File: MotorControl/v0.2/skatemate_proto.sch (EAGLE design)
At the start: 97 parts, among them IC1 REG1117, U1 DRV8301DCAR, U2 STM32F303XD/XELQFP64, X1 ABM3B

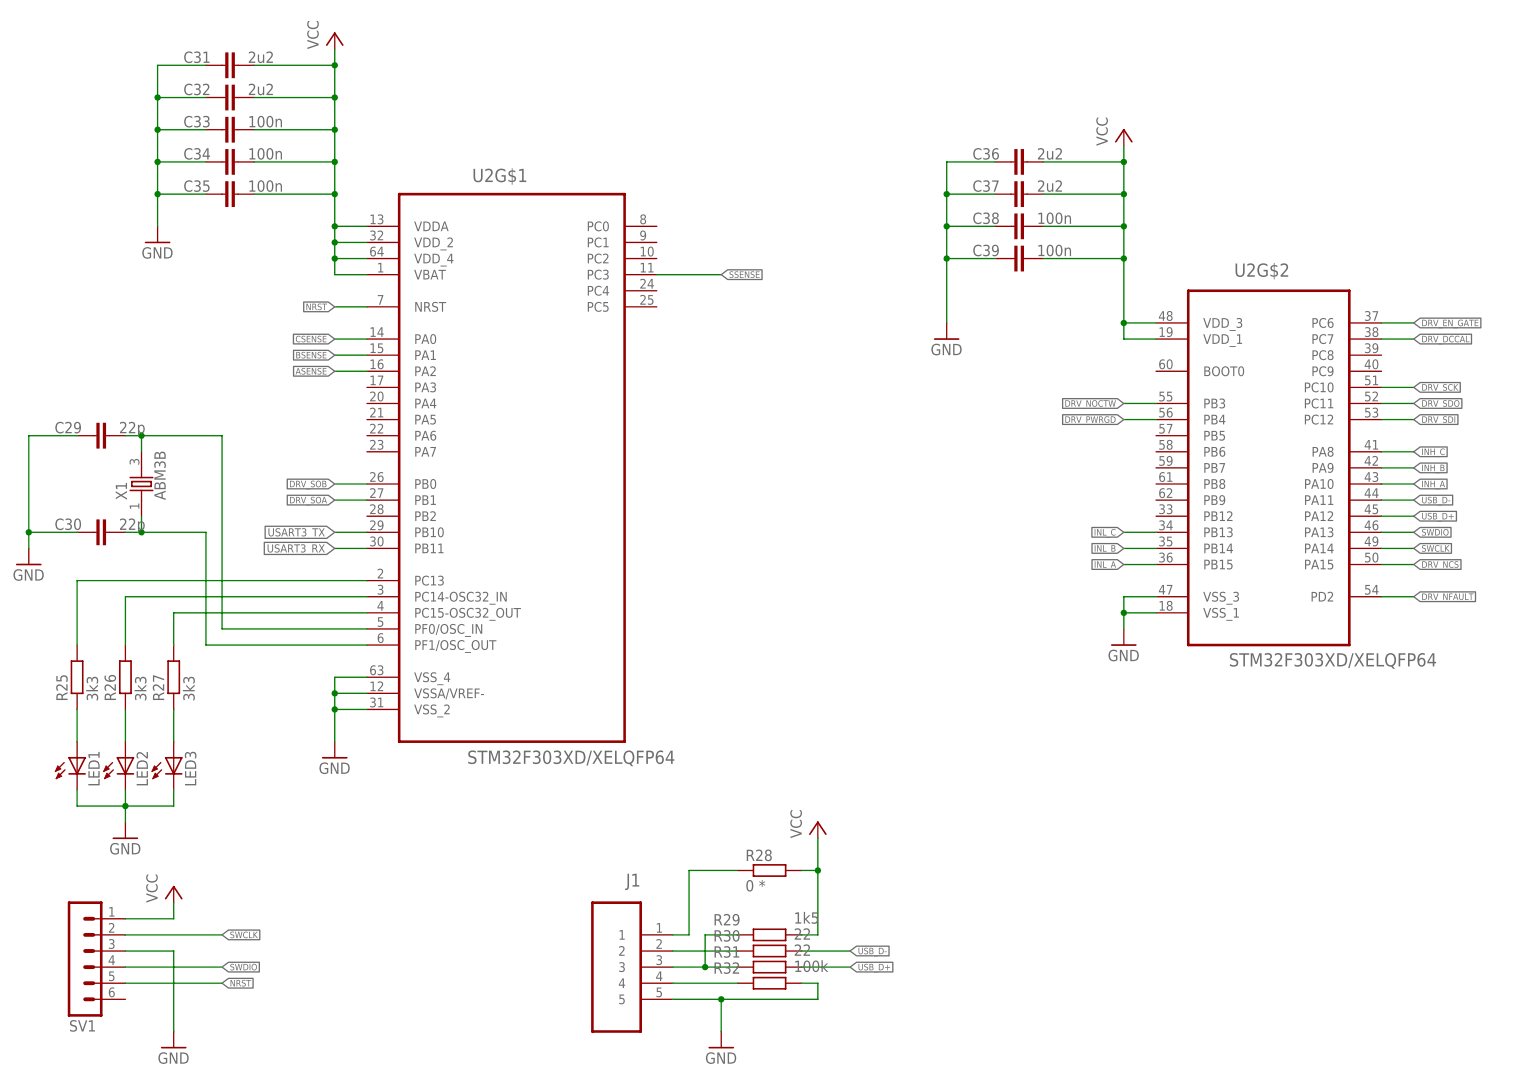
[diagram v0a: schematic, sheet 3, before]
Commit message: Add RFM module
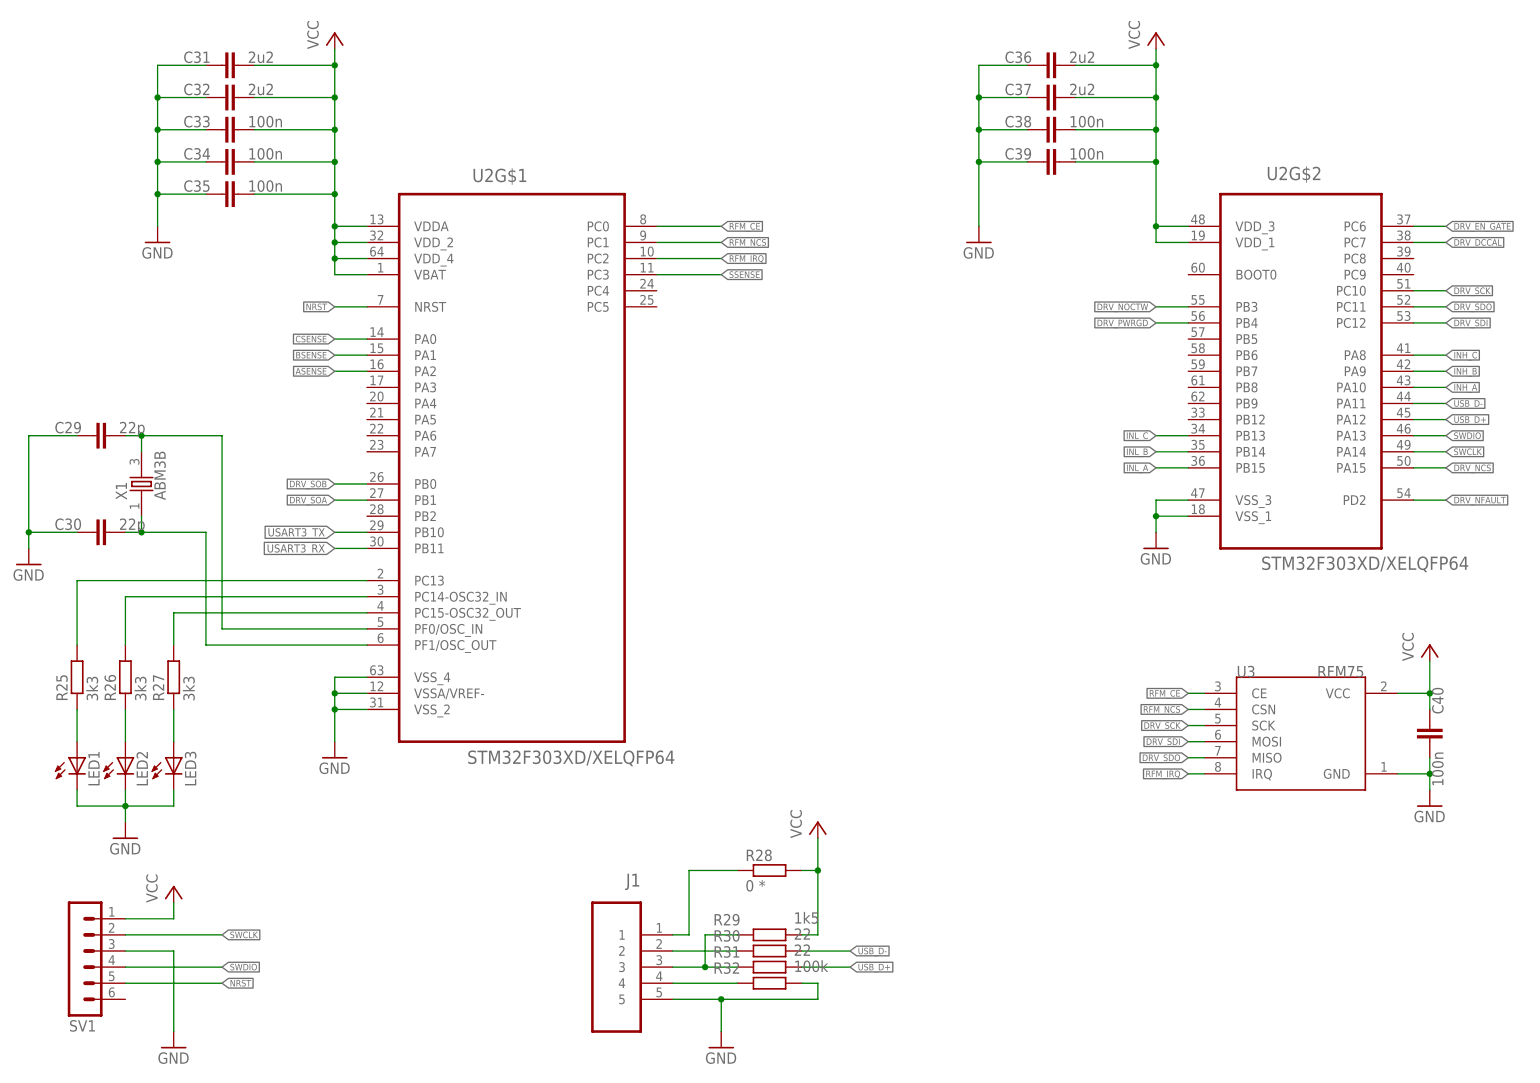
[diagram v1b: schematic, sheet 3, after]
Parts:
- added C40: 100n, skatemate:C-EUC0805
- added U3: RFM75, skatemate:RFM75
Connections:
- new net RFM_CE: U2G$1.PC0, U3.CE
- new net RFM_IRQ: U2G$1.PC2, U3.IRQ
- new net RFM_NCS: U2G$1.PC1, U3.CSN
- net DRV_SCK: now also U3.SCK
- net DRV_SDI: now also U3.MOSI
- net DRV_SDO: now also U3.MISO
- net GND: now also C40.2, U3.GND
- net VCC: now also C40.1, U3.VCC
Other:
- moved on the sheet: C36, C37, C38, C39, U2G$2

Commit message: finished all wires and first review
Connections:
- net RFM_CE: now also U2G$1.PC2; no longer U2G$1.PC0
- net RFM_IRQ: now also U2G$1.PC0; no longer U2G$1.PC2
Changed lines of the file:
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@@
 </segment>
 <segment>
-<pinref part="U2" gate="G$1" pin="PC0"/>
-<wire x1="101.6" y1="142.24" x2="111.76" y2="142.24" width="0.1524" layer="91"/>
-<label x="111.76" y="142.24" size="1.016" layer="95" xref="yes"/>
+<pinref part="U2" gate="G$1" pin="PC2"/>
+<wire x1="101.6" y1="137.16" x2="111.76" y2="137.16" width="0.1524" layer="91"/>
+<label x="111.76" y="137.16" size="1.016" layer="95" xref="yes"/>
 </segment>
 </net>
@@
 </segment>
 <segment>
-<pinref part="U2" gate="G$1" pin="PC2"/>
-<wire x1="101.6" y1="137.16" x2="111.76" y2="137.16" width="0.1524" layer="91"/>
-<label x="111.76" y="137.16" size="1.016" layer="95" xref="yes"/>
+<pinref part="U2" gate="G$1" pin="PC0"/>
+<wire x1="101.6" y1="142.24" x2="111.76" y2="142.24" width="0.1524" layer="91"/>
+<label x="111.76" y="142.24" size="1.016" layer="95" xref="yes"/>
 </segment>
 </net>

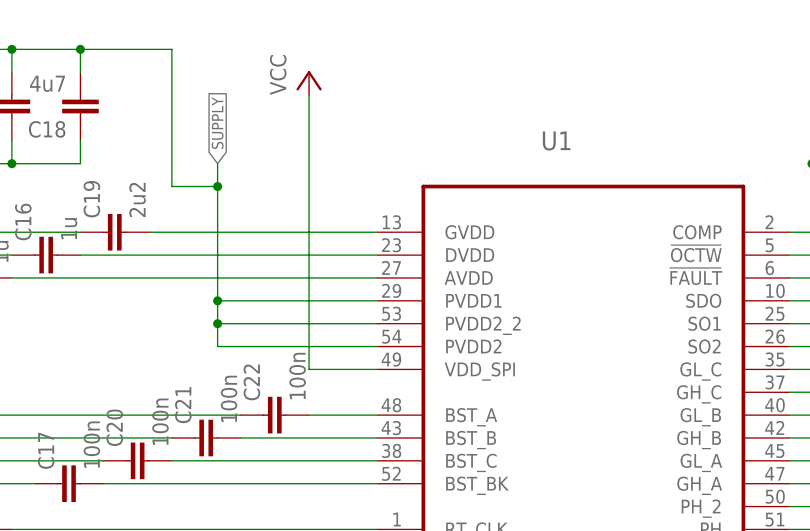
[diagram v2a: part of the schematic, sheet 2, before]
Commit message: Layout angepasst
C ergänzt
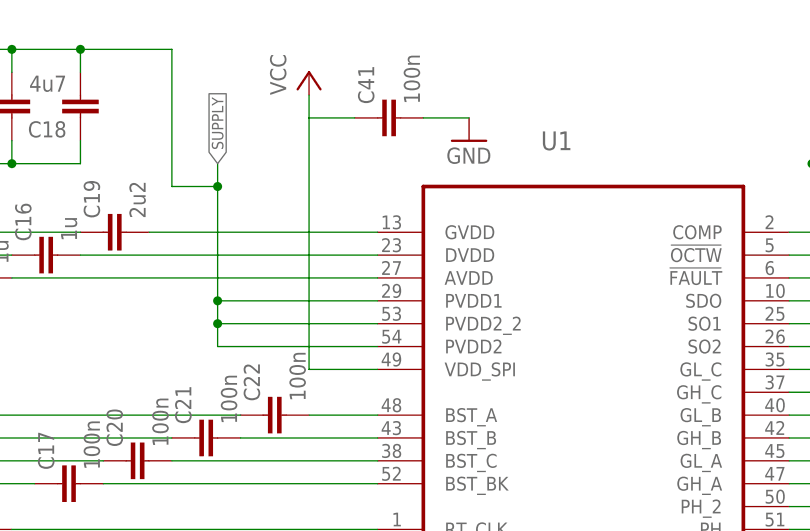
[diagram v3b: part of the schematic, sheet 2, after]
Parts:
- added C41: 100n, skatemate:C-EUC0805
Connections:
- net GND: now also C41.2
- net VCC: now also C41.1
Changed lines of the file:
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@@
 <part name="P+13" library="supply1" deviceset="VCC" device=""/>
 <part name="C40" library="skatemate" deviceset="C-EU" device="C0805" value="100n"/>
+<part name="C41" library="skatemate" deviceset="C-EU" device="C0805" value="100n"/>
+<part name="GND21" library="supply1" deviceset="GND" device=""/>
 </parts>
 <sheets>
@@
 <instance part="C24" gate="G$1" x="139.7" y="172.72" rot="R90"/>
 <instance part="GND9" gate="1" x="160.02" y="160.02"/>
+<instance part="C41" gate="G$1" x="78.74" y="170.18" rot="R90"/>
+<instance part="GND21" gate="1" x="88.9" y="167.64"/>
 </instances>
 <busses>
@@
 <label x="66.04" y="53.34" size="1.27" layer="95" rot="R180" xref="yes"/>
 </segment>
+<segment>
+<pinref part="GND21" gate="1" pin="GND"/>
+<pinref part="C41" gate="G$1" pin="2"/>
+<wire x1="88.9" y1="170.18" x2="83.82" y2="170.18" width="0.1524" layer="91"/>
+</segment>
 </net>
 <net name="SN_A" class="0">
@@
 <pinref part="P+5" gate="VCC" pin="VCC"/>
 <wire x1="78.74" y1="142.24" x2="71.12" y2="142.24" width="0.1524" layer="91"/>
-<wire x1="71.12" y1="142.24" x2="71.12" y2="172.72" width="0.1524" layer="91"/>
-</segment>
-<segment>
+<wire x1="71.12" y1="142.24" x2="71.12" y2="170.18" width="0.1524" layer="91"/>
+<pinref part="C41" gate="G$1" pin="1"/>
+<wire x1="71.12" y1="170.18" x2="71.12" y2="172.72" width="0.1524" layer="91"/>
+<wire x1="76.2" y1="170.18" x2="71.12" y2="170.18" width="0.1524" layer="91"/>
+</segment>
+<segment>

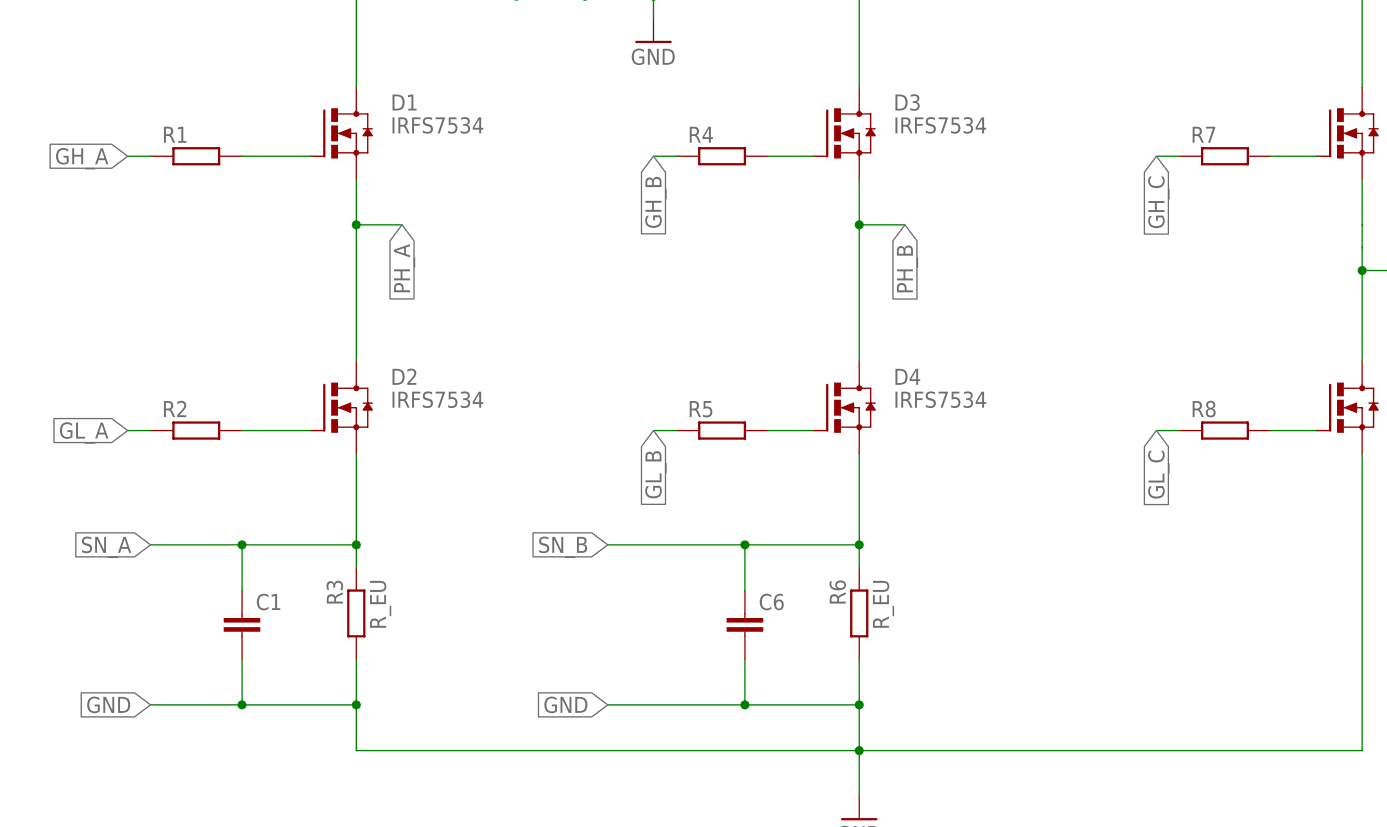
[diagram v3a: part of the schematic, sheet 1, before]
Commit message: Added missing values
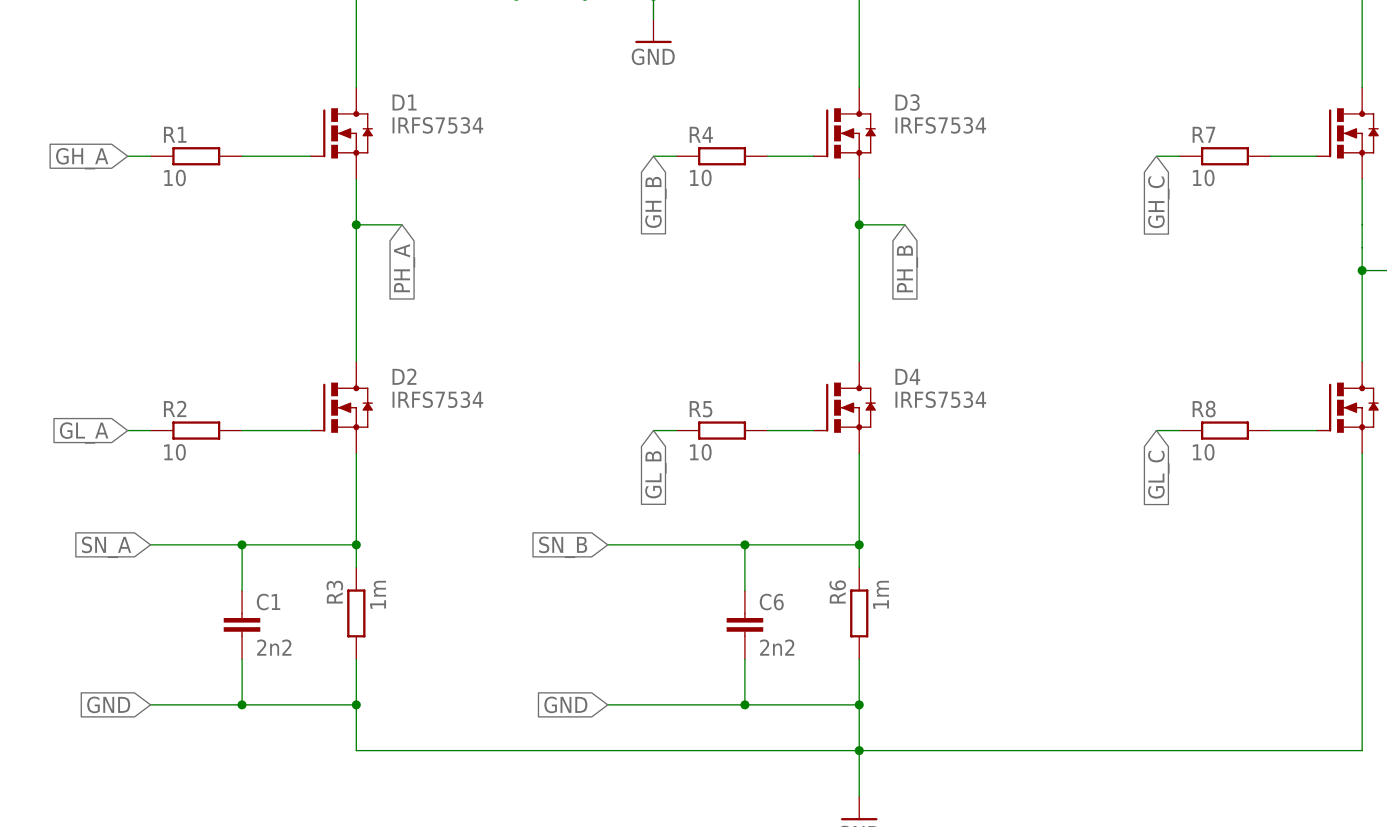
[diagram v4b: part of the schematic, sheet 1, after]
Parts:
- C1, C6: value (none) -> 2n2
- C23: value (none) -> 22n
- R1, R2, R4, R5, R7, R8: value (none) -> 10
- R3, R6: value R_EU -> 1m
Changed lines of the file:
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@@
 <parts>
 <part name="U1" library="skatemate" deviceset="DRV8301DCAR" device=""/>
-<part name="R1" library="skatemate" deviceset="R-EU_" device="R0805"/>
-<part name="R2" library="skatemate" deviceset="R-EU_" device="R0805"/>
-<part name="R4" library="skatemate" deviceset="R-EU_" device="R0805"/>
-<part name="R5" library="skatemate" deviceset="R-EU_" device="R0805"/>
-<part name="R7" library="skatemate" deviceset="R-EU_" device="R0805"/>
-<part name="R8" library="skatemate" deviceset="R-EU_" device="R0805"/>
-<part name="R3" library="skatemate" deviceset="R_EU" device=""/>
-<part name="R6" library="skatemate" deviceset="R_EU" device=""/>
+<part name="R1" library="skatemate" deviceset="R-EU_" device="R0805" value="10"/>
+<part name="R2" library="skatemate" deviceset="R-EU_" device="R0805" value="10"/>
+<part name="R4" library="skatemate" deviceset="R-EU_" device="R0805" value="10"/>
+<part name="R5" library="skatemate" deviceset="R-EU_" device="R0805" value="10"/>
+<part name="R7" library="skatemate" deviceset="R-EU_" device="R0805" value="10"/>
+<part name="R8" library="skatemate" deviceset="R-EU_" device="R0805" value="10"/>
+<part name="R3" library="skatemate" deviceset="R_EU" device="" value="1m"/>
+<part name="R6" library="skatemate" deviceset="R_EU" device="" value="1m"/>
 <part name="GND3" library="supply1" deviceset="GND" device=""/>
-<part name="C1" library="skatemate" deviceset="C-EU" device="C0805"/>
-<part name="C6" library="skatemate" deviceset="C-EU" device="C0805"/>
+<part name="C1" library="skatemate" deviceset="C-EU" device="C0805" value="2n2"/>
+<part name="C6" library="skatemate" deviceset="C-EU" device="C0805" value="2n2"/>
 <part name="R9" library="skatemate" deviceset="R-EU_" device="R0805" value="39k"/>
 <part name="R10" library="skatemate" deviceset="R-EU_" device="R0805" value="2k2"/>
@@
 <part name="FRAME2" library="frames" deviceset="DINA4_L" device=""/>
 <part name="GND8" library="supply1" deviceset="GND" device=""/>
-<part name="C23" library="skatemate" deviceset="C-EU" device="C0805"/>
+<part name="C23" library="skatemate" deviceset="C-EU" device="C0805" value="22n"/>
 <part name="P+6" library="supply1" deviceset="VCC" device=""/>
 <part name="R20" library="skatemate" deviceset="R-EU_" device="R0805" value="10k"/>
